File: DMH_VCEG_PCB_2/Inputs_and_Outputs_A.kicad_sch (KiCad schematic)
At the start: 35 parts, among them J1 TS_Jack_6.35mm_Sw, J10 TS_Jack_6.35mm_Sw, J2 TS_Jack_6.35mm_Sw, J200 IDC_02x08, J21 Conn_01x10_PinHeader, J22 Conn_01x10_PinHeader, J23 Conn_01x10_PinHeader, J27 Conn_01x06_PinHeader, J3 TS_Jack_6.35mm_Sw, J4 TS_Jack_6.35mm_Sw, J5 TS_Jack_6.35mm_Sw, J6 TS_Jack_6.35mm_Sw, J7 TS_Jack_6.35mm_Sw, J8 TS_Jack_6.35mm_Sw, J9 TS_Jack_6.35mm_Sw, U21 TL072, U9 TL074

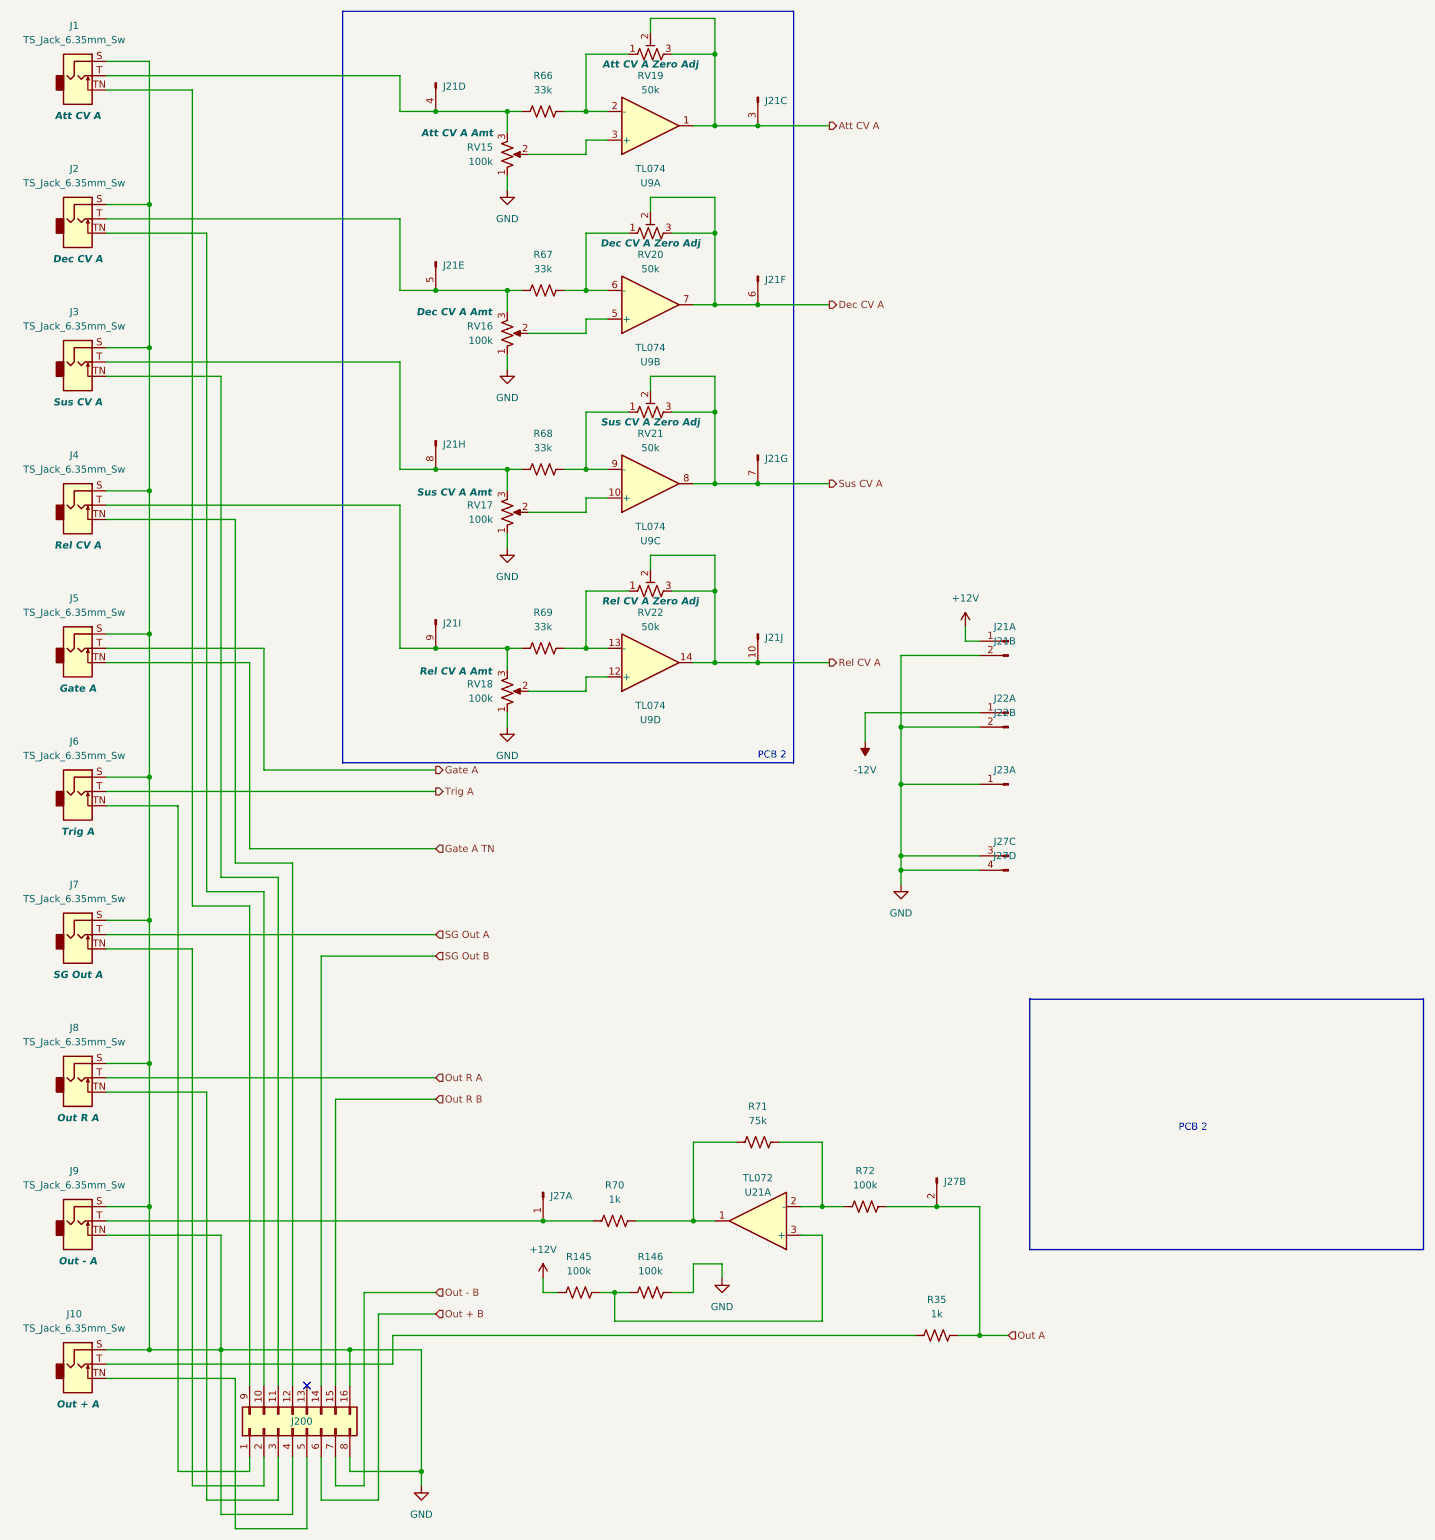
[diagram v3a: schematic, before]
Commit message: Added Output attenuation circuit
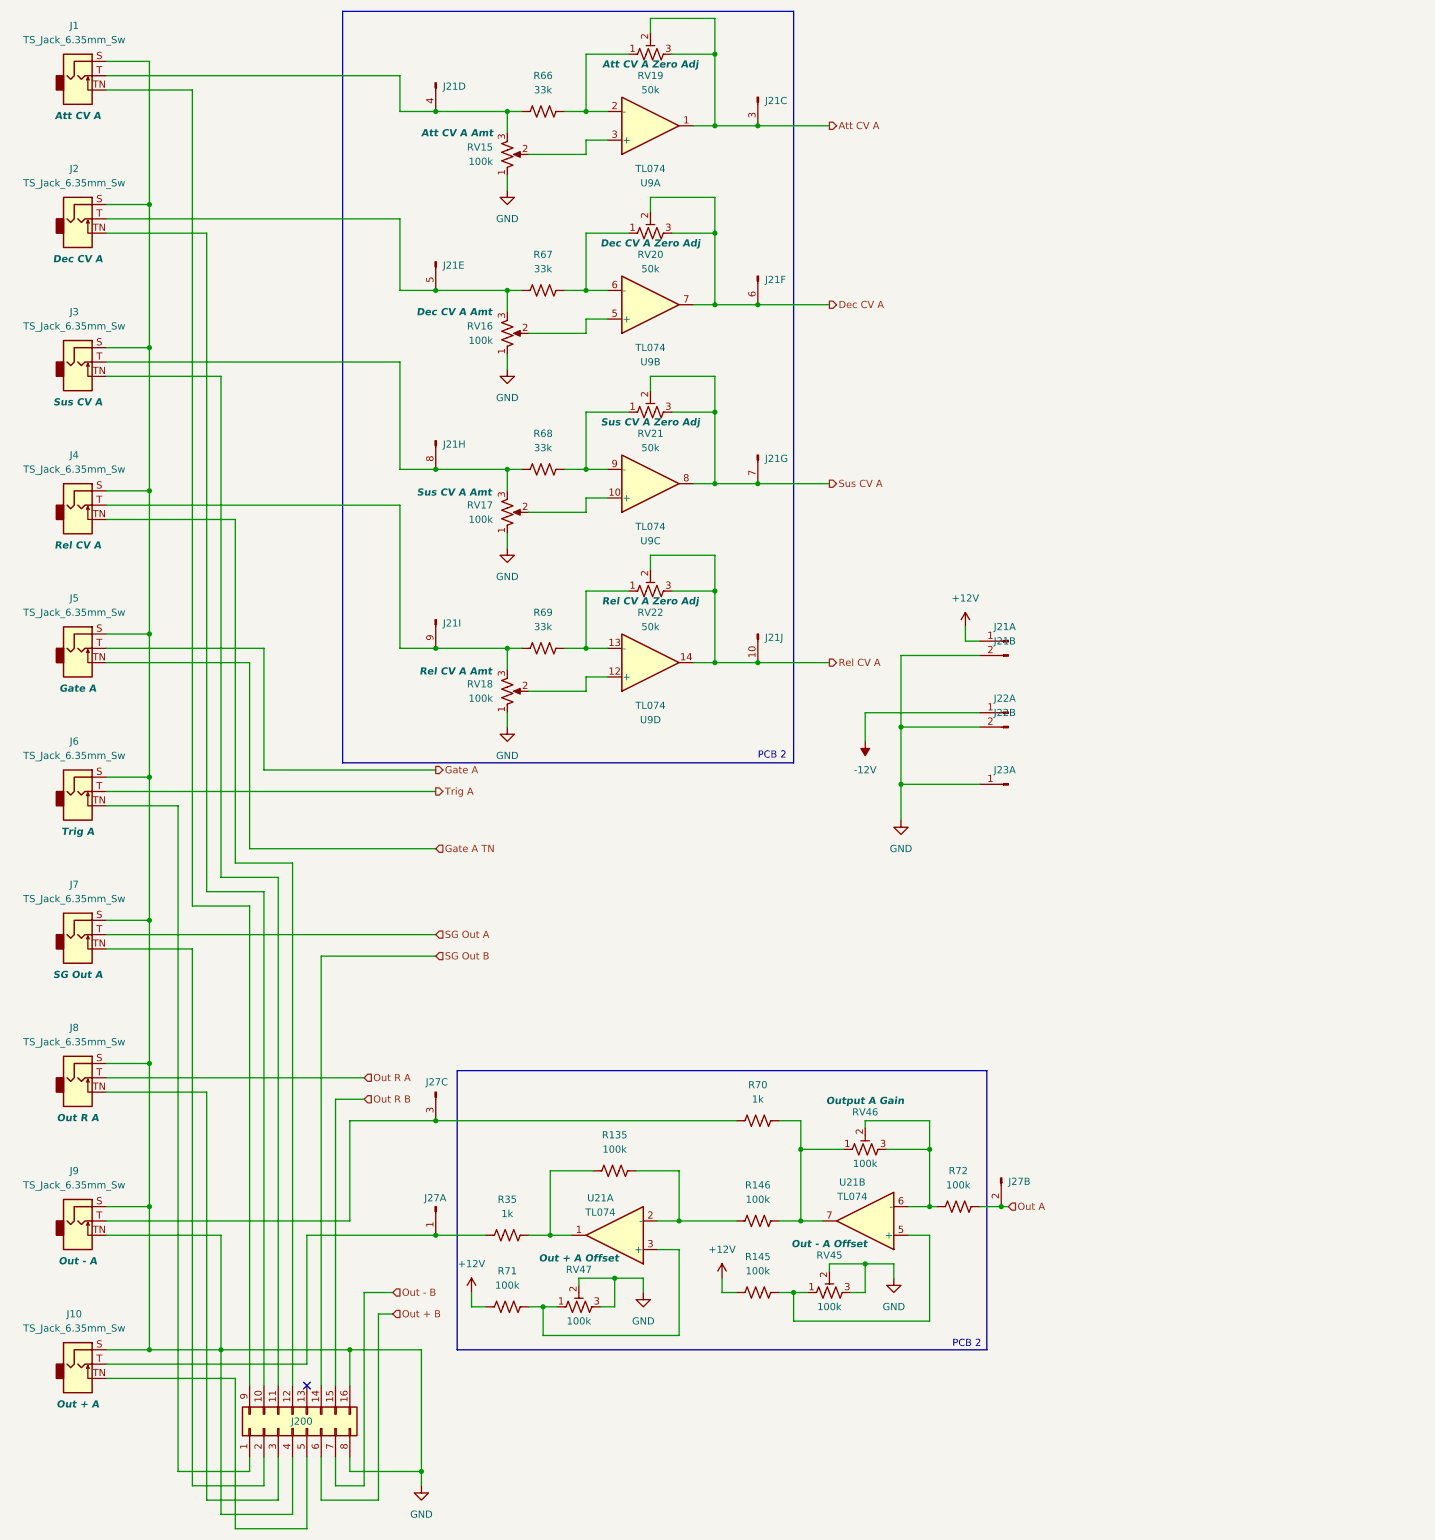
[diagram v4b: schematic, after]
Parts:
- removed unit 4 of J27
- removed U21: TL072, Package_DIP:DIP-8_W7.62mm_Socket, symbol Amplifier_Operational:TL072
- added R135: 100k, Resistor_THT:R_Axial_DIN0207_L6.3mm_D2.5mm_P7.62mm_Horizontal, symbol Device:R_US
- added RV45, RV46, RV47: 100k, Potentiometer_THT:Potentiometer_Bourns_3296X_Horizontal, symbol Device:R_Potentiometer_Trim_US
- added U21: TL074, symbol Amplifier_Operational:TL074
- R71: value 75k -> 100k
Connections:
- net +12V: now also R71.2
- net GND: now also RV45.2, RV45.3, RV47.2, RV47.3; no longer J27.3 (Pin_3), R146.1
- net Out A: no longer R35.1
- net at R72.2: now also RV46.2, RV46.3, U21.6 (-); no longer R71.1
- net at J9.T, R70.2: now also J27.3 (Pin_3); no longer J27.1 (Pin_1)
- net at J10.T, R35.2: now also J27.1 (Pin_1)
- net at R70.1: now also R146.1, RV46.1, U21.7; no longer R71.2
- net at R146.2: now also R135.1, U21.2 (-); no longer R145.1
- new net: R135.2, R35.1, U21.1
- new net: R145.1, RV45.1, U21.5 (+)
- new net: R71.1, RV47.1, U21.3 (+)
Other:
- moved on the sheet: J27B, J27C, R145, R35, R70, R72
